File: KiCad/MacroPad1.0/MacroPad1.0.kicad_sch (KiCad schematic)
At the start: 2 parts

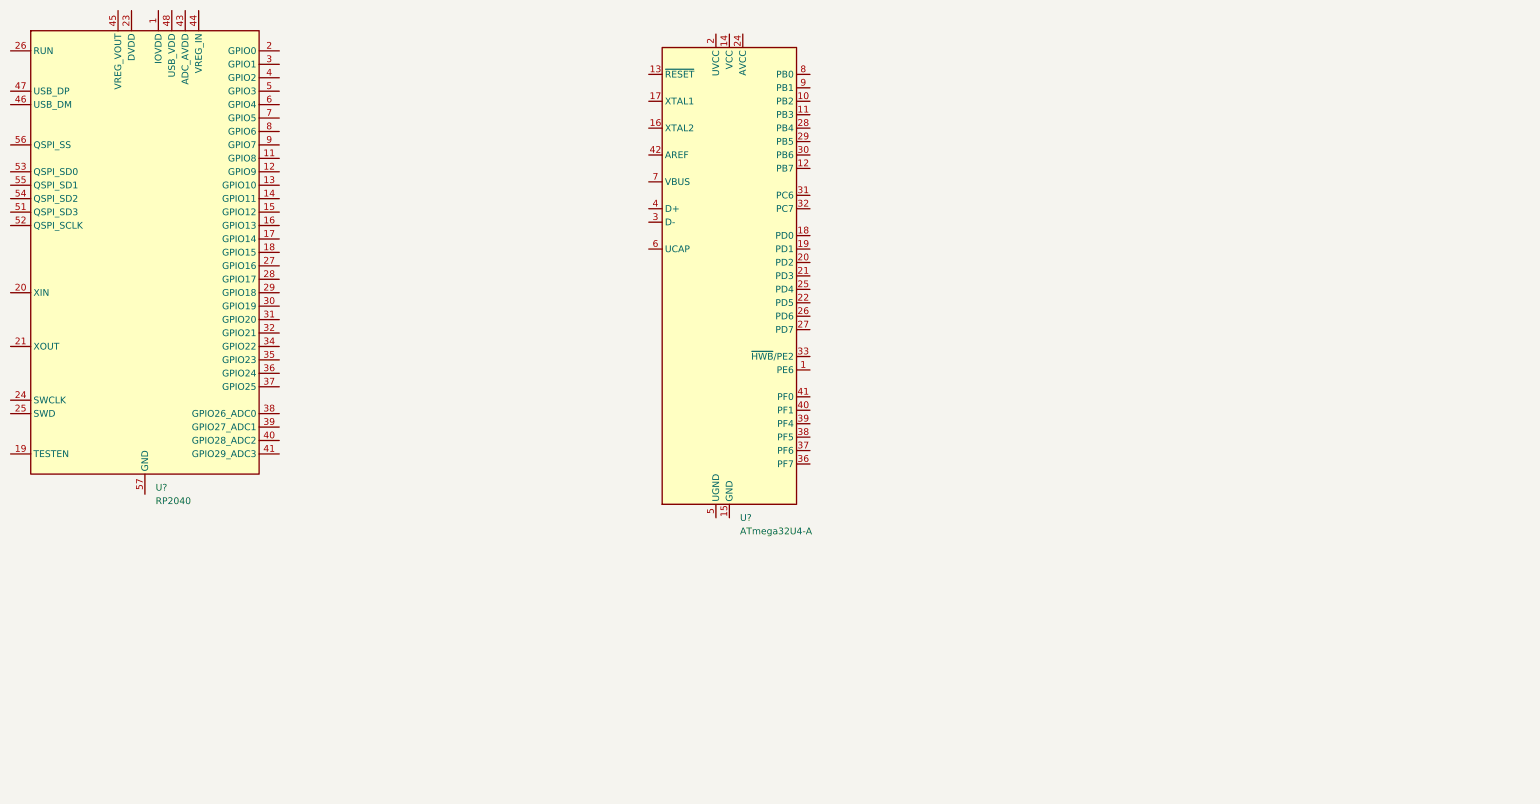
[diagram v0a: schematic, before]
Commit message: Added MCU Schematic
Wiring for ATMEGA32U4
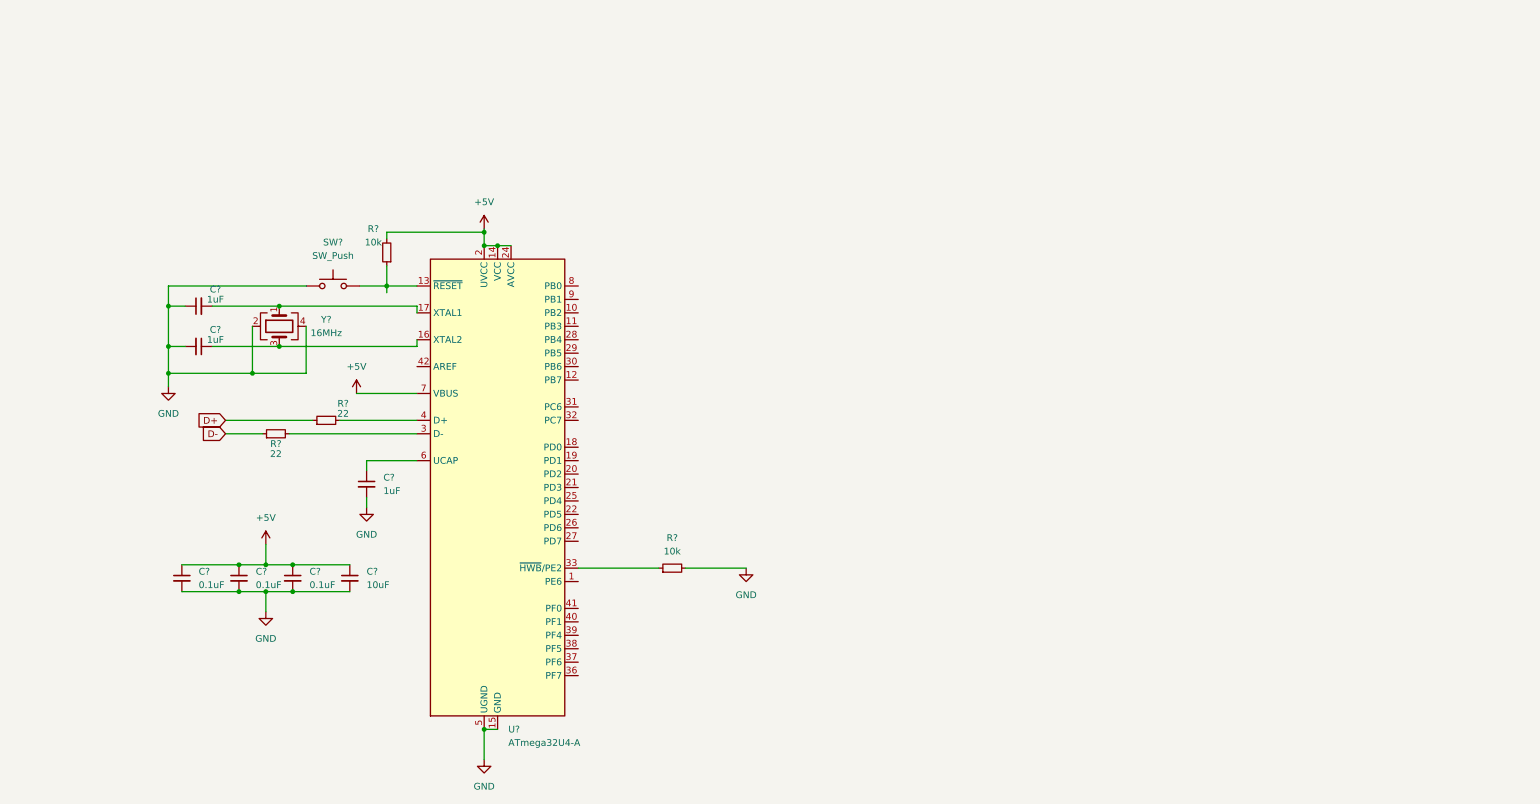
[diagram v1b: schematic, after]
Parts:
- removed U?: RP2040, Package_DFN_QFN:QFN-56-1EP_7x7mm_P0.4mm_EP3.2x3.2mm, symbol MCU_RaspberryPi:RP2040
- added C? (x3): 1uF, symbol Device:C_Small
- added C? (x3): 0.1uF, symbol Device:C_Small
- added C?: 10uF, symbol Device:C_Small
- added R? (x2): 10k, symbol Device:R_Small
- added R? (x2): 22, symbol Device:R_Small
- added SW?: SW_Push, symbol Switch:SW_Push
- added Y?: 16MHz, symbol Device:Crystal_GND24
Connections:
- net at U?.13 (~{RESET}): now also R?.1, SW?.2
- net +5V: now reaches U?.14 (VCC), U?.34 (VCC)
- net +5V: now also U?.2 (UVCC), U?.24 (AVCC), U?.44 (AVCC), U?.7 (VBUS), C?.1, C?.1, C?.1, C?.1, R?.2
- net GND: now reaches U?.15 (GND), U?.23 (GND), U?.35 (GND), U?.43 (GND)
- net GND: now also U?.5 (UGND), C?.1, C?.2, C?.2, C?.2, C?.2, C?.2, C?.2, R?.2, SW?.1, Y?.2, Y?.4
- net at U?.16 (XTAL2): now also C?.1, Y?.3
- net at U?.17 (XTAL1): now also C?.2, Y?.1
- net at U?.3 (D-): now also R?.2
- net at U?.33 (~{HWB}/PE2): now also R?.1
- net at U?.4 (D+): now also R?.2
- net at U?.6 (UCAP): now also C?.1
- new net D+: R?.1
- new net D-: R?.1
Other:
- moved on the sheet: U?

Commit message: Added USB and Switches
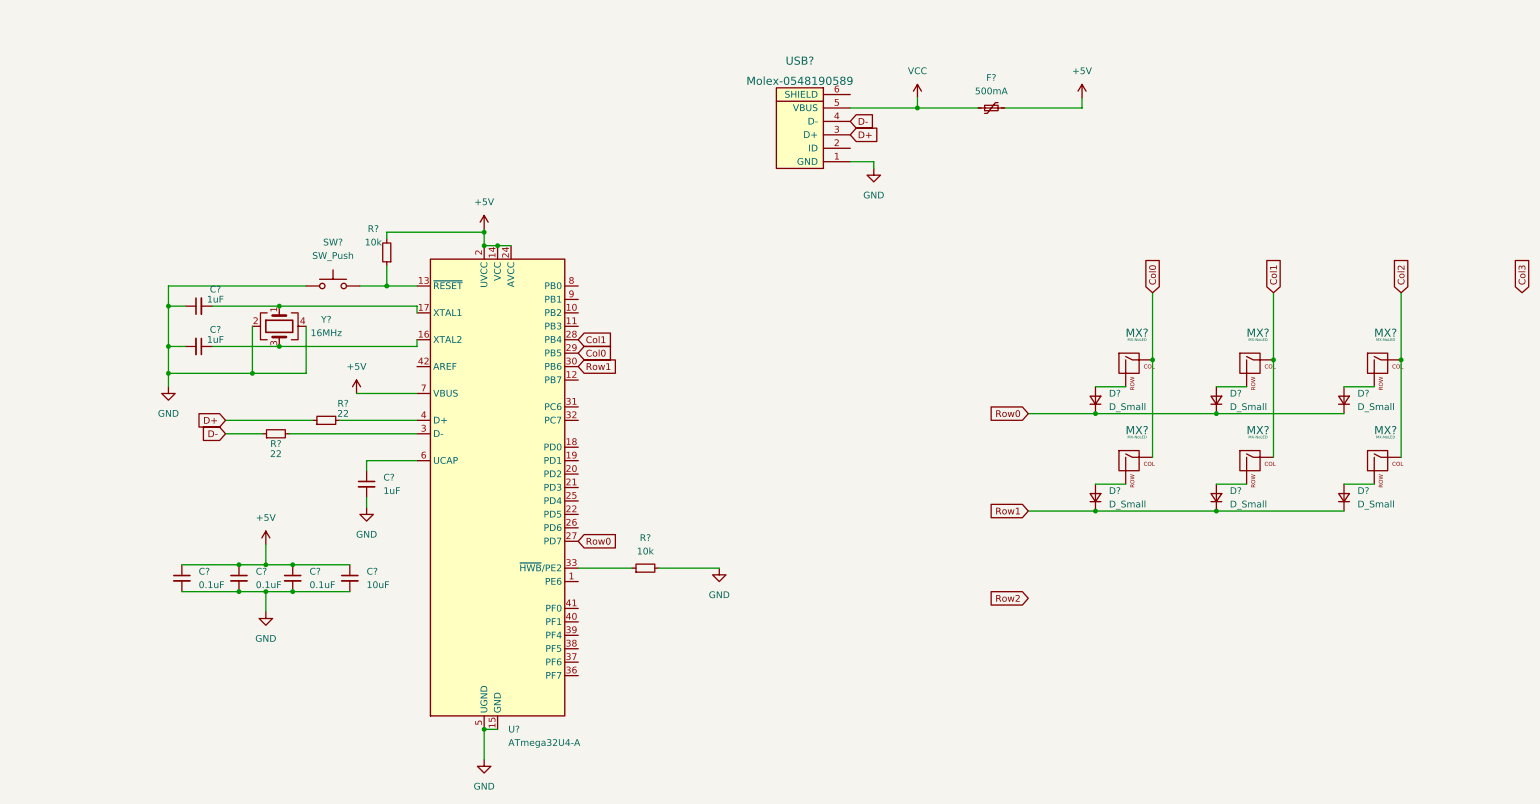
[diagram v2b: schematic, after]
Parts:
- added D? (x6): D_Small, symbol Device:D_Small
- added F?: 500mA, symbol Device:Polyfuse_Small
- added MX? (x6): MX-NoLED, symbol MX_Alps_Hybrid:MX-NoLED
- added USB?: Molex-0548190589, symbol random-keyboard-parts:Molex-0548190589
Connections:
- net +5V: now also F?.2
- net D+: now also USB?.3 (D+)
- net D-: now also USB?.4 (D-)
- net GND: now also USB?.1 (GND)
- net Row0: now reaches U?.27 (PD7)
- net Row0: now also D?.1 (K), D?.1 (K), D?.1 (K)
- net Col1: now reaches U?.28 (PB4)
- net Col1: now also MX?.1 (COL), MX?.1 (COL)
- net Col0: now reaches U?.29 (PB5)
- net Col0: now also MX?.1 (COL), MX?.1 (COL)
- net Row1: now reaches U?.30 (PB6)
- net Row1: now also D?.1 (K), D?.1 (K), D?.1 (K)
- new net: D?.2 (A), MX?.2 (ROW) (x6)
- new net Col2: MX?.1 (COL), MX?.1 (COL)
- new net VCC: F?.1, USB?.5 (VBUS)
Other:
- moved on the sheet: R?

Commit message: Assigned Footprints
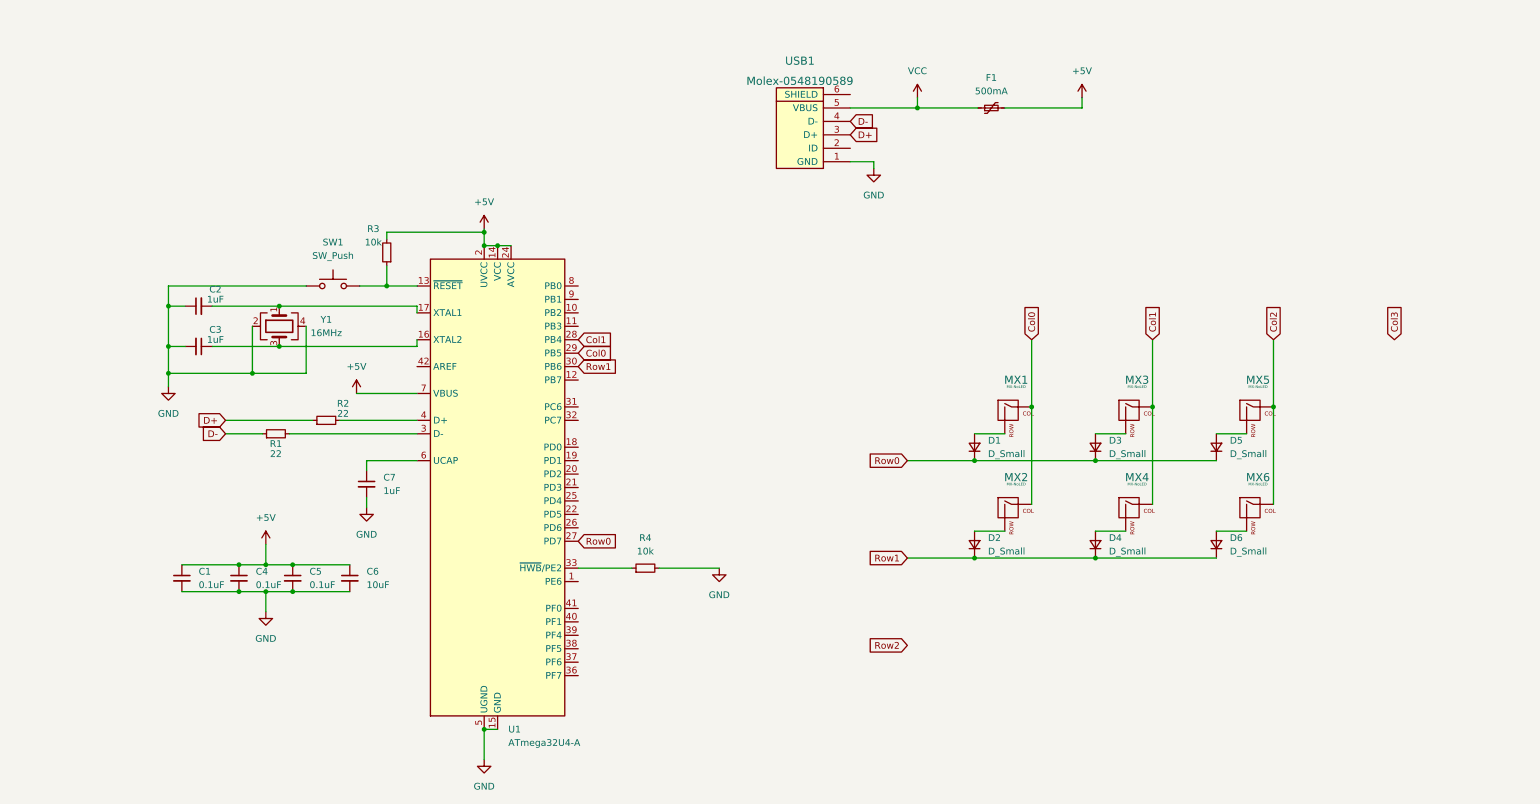
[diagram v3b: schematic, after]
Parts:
- C1, C2, C3, C4, C5, C6, C7: renamed from C?; footprint (none) -> Capacitor_SMD:C_0805_2012Metric
- D1, D2, D3, D4, D5, D6: renamed from D?; footprint (none) -> Diode_SMD:D_SOD-123
- F1: renamed from F?; footprint (none) -> Fuse:Fuse_1206_3216Metric
- MX1, MX2, MX3, MX4, MX5, MX6: renamed from MX?; footprint (none) -> MX_Alps_Hybrid:MX-1U-NoLED
- R1, R2, R3, R4: renamed from R?; footprint (none) -> Resistor_SMD:R_0805_2012Metric
- SW1: renamed from SW?; footprint (none) -> random-keyboard-parts:SKQG-1155865
- USB1: renamed from USB?; footprint (none) -> random-keyboard-parts:Molex-0548190589
- Y1: renamed from Y?; footprint (none) -> Crystal:Crystal_SMD_3225-4Pin_3.2x2.5mm
- gave numbers to parts that had none: 1
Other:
- moved on the sheet: D1, D2, D3, D4, D5, D6, MX1, MX2, MX3, MX4, MX5, MX6

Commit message: PCB traces complete
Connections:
- net Col2: now also U1.26 (PD6)
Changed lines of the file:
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@@
     )
   )
-  (global_label "Col3" (shape input) (at 294.005 91.44 90) (fields_autoplaced)
+  (global_label "Col2" (shape input) (at 139.7 127 0) (fields_autoplaced)
     (effects (font (size 1.27 1.27)) (justify left))
-    (property "Intersheet References" "${INTERSHEET_REFS}" (id 0) (at 293.9256 84.7331 90)
+    (property "Intersheet References" "${INTERSHEET_REFS}" (id 0) (at 146.4069 126.9206 0)
       (effects (font (size 1.27 1.27)) (justify left) hide)
     )
@@
       (effects (font (size 1.27 1.27)) (justify right) hide)
     )
-  )
-  (global_label "Row2" (shape input) (at 201.93 149.225 180) (fields_autoplaced)
-    (effects (font (size 1.27 1.27)) (justify right))
-    (property "Intersheet References" "${INTERSHEET_REFS}" (id 0) (at 194.5579 149.1456 0)
-      (effects (font (size 1.27 1.27)) (justify right) hide)
-    )

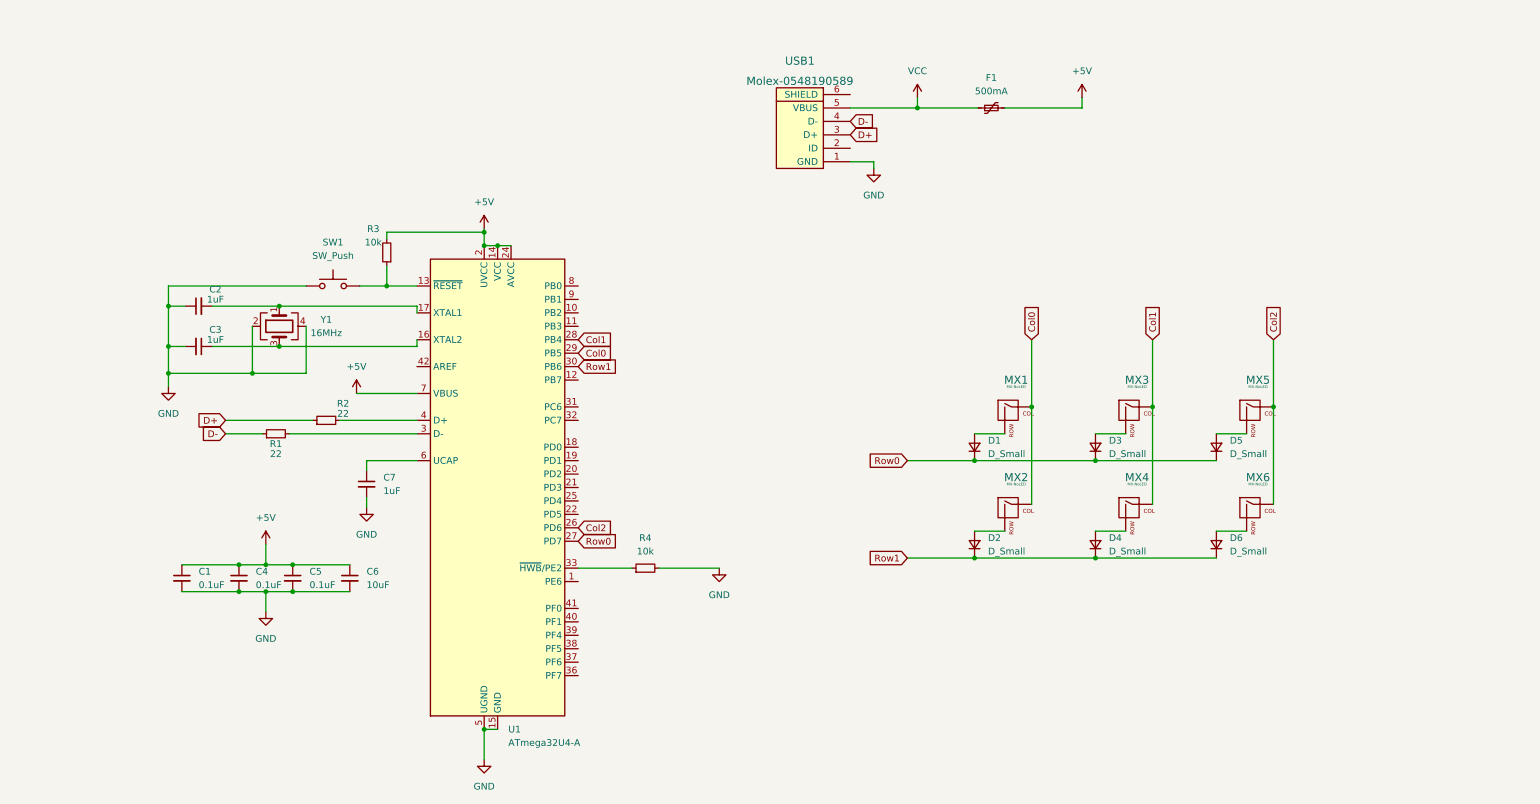
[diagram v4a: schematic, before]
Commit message: Adjusted page size
and also rearranged symbols
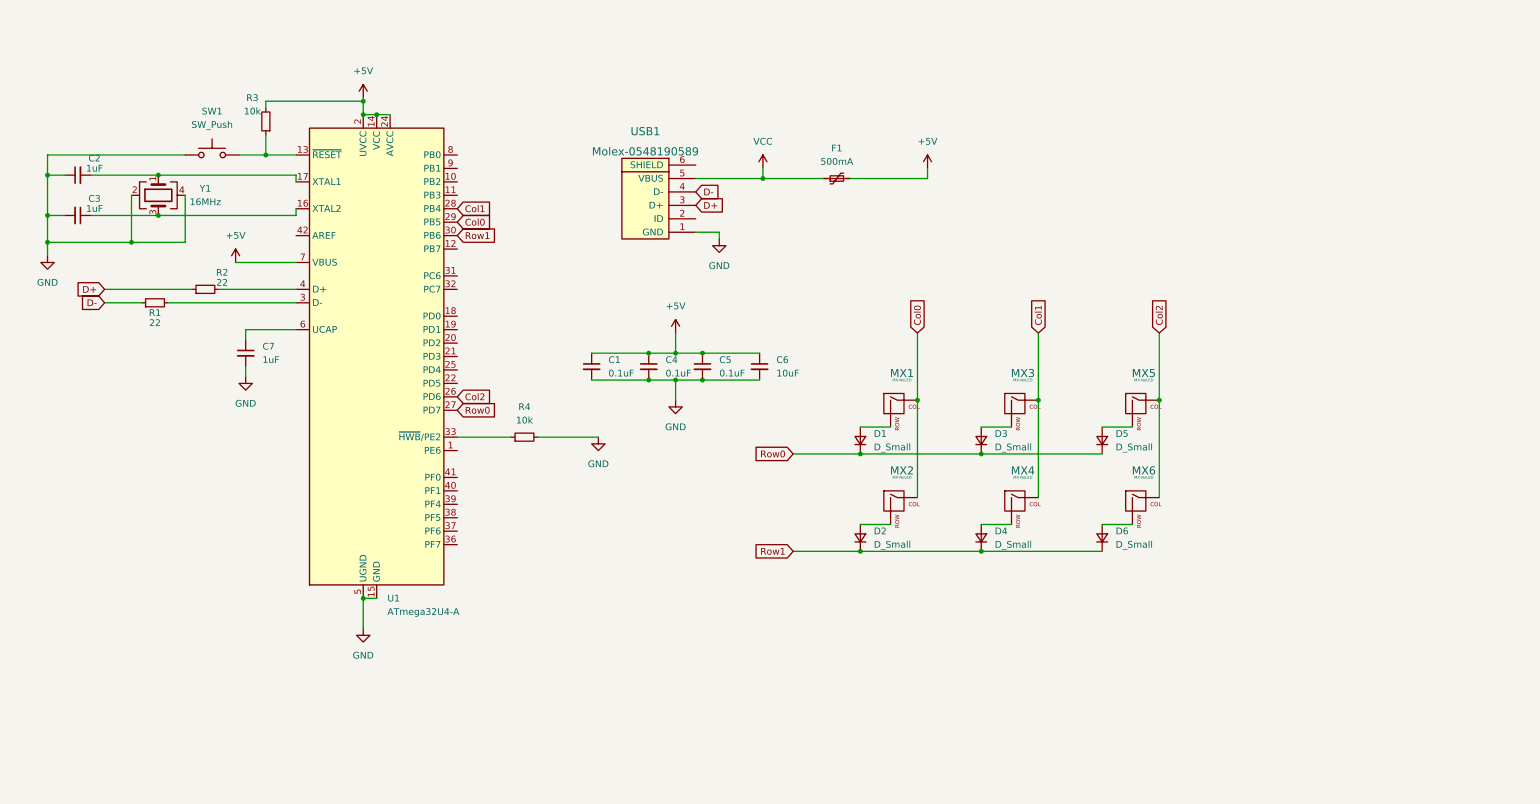
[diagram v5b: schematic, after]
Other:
- moved on the sheet: C1, C2, C3, C4, C5, C6, C7, D1, D2, D3, D4, D5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

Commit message: Documentation Updates
Updated HTML BOM, small additions to README
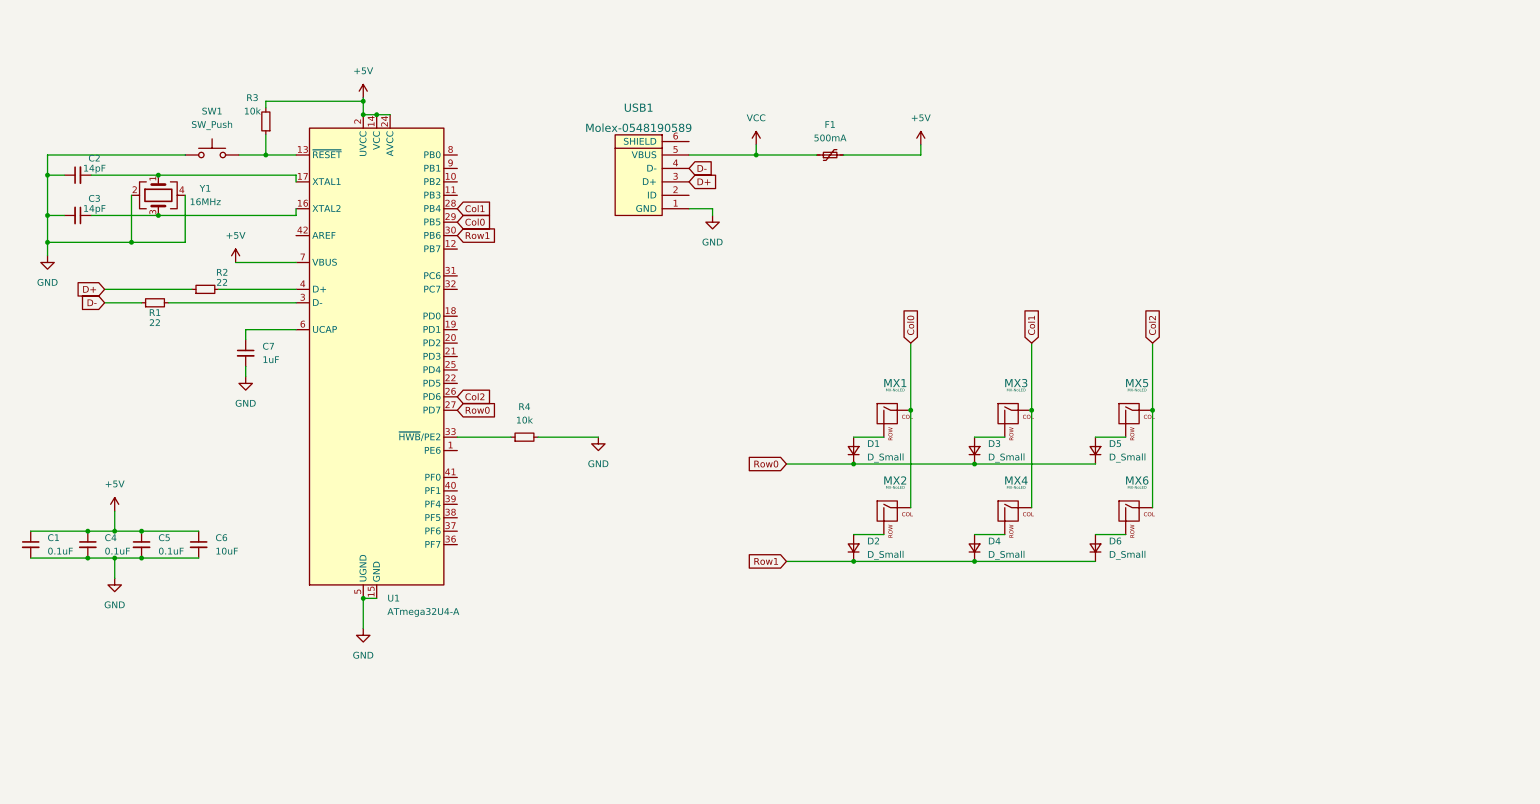
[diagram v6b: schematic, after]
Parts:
- C2, C3: value 1uF -> 14pF
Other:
- moved on the sheet: C1, C4, C5, C6, D1, D2, D3, D4, D5, D6, F1, MX1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
